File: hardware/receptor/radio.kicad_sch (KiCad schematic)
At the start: 5 parts, among them U2 E220-900T30D

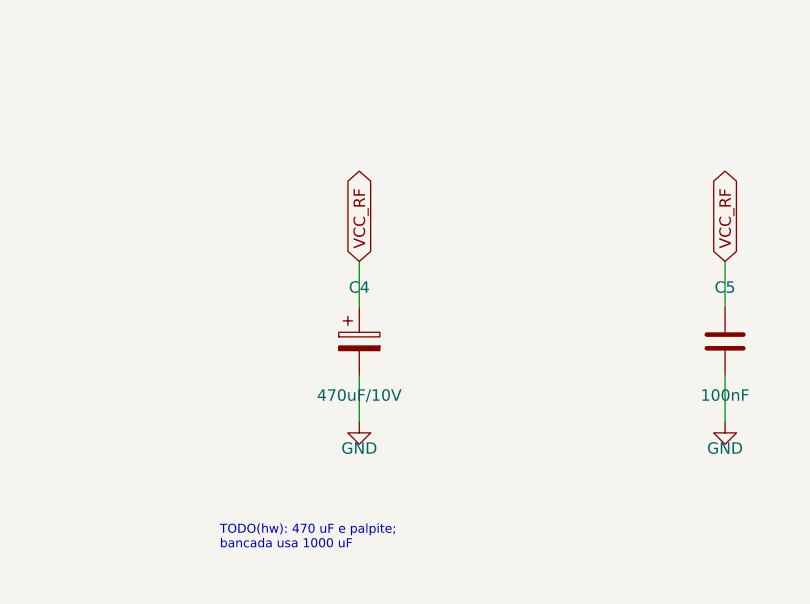
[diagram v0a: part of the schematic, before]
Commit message: wip(hw): roteador proprio, layout v2 com pecas sob o E220 (checkpoint antes de trocar para jack 12 V)
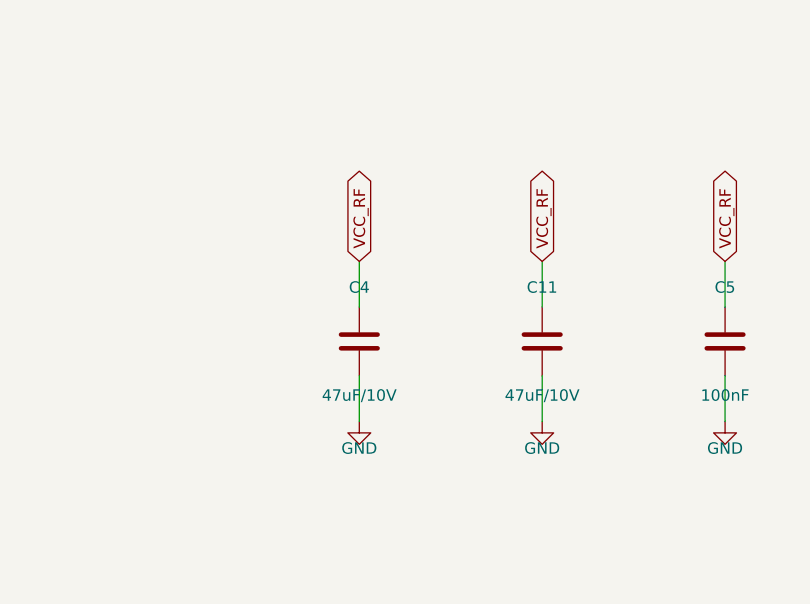
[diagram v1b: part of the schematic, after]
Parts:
- removed C4: 470uF/10V, Capacitor_SMD:CP_Elec_8x10.5, symbol Device:C_Polarized
- added C11, C4: 47uF/10V, Capacitor_SMD:C_1210_3225Metric, symbol Device:C
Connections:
- net GND: now also C11.2, C4.2
- net VCC_RF: now also C11.1, C4.1
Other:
- note removed: "TODO(hw): 470 uF e palpite; bancada usa 1000 uF"

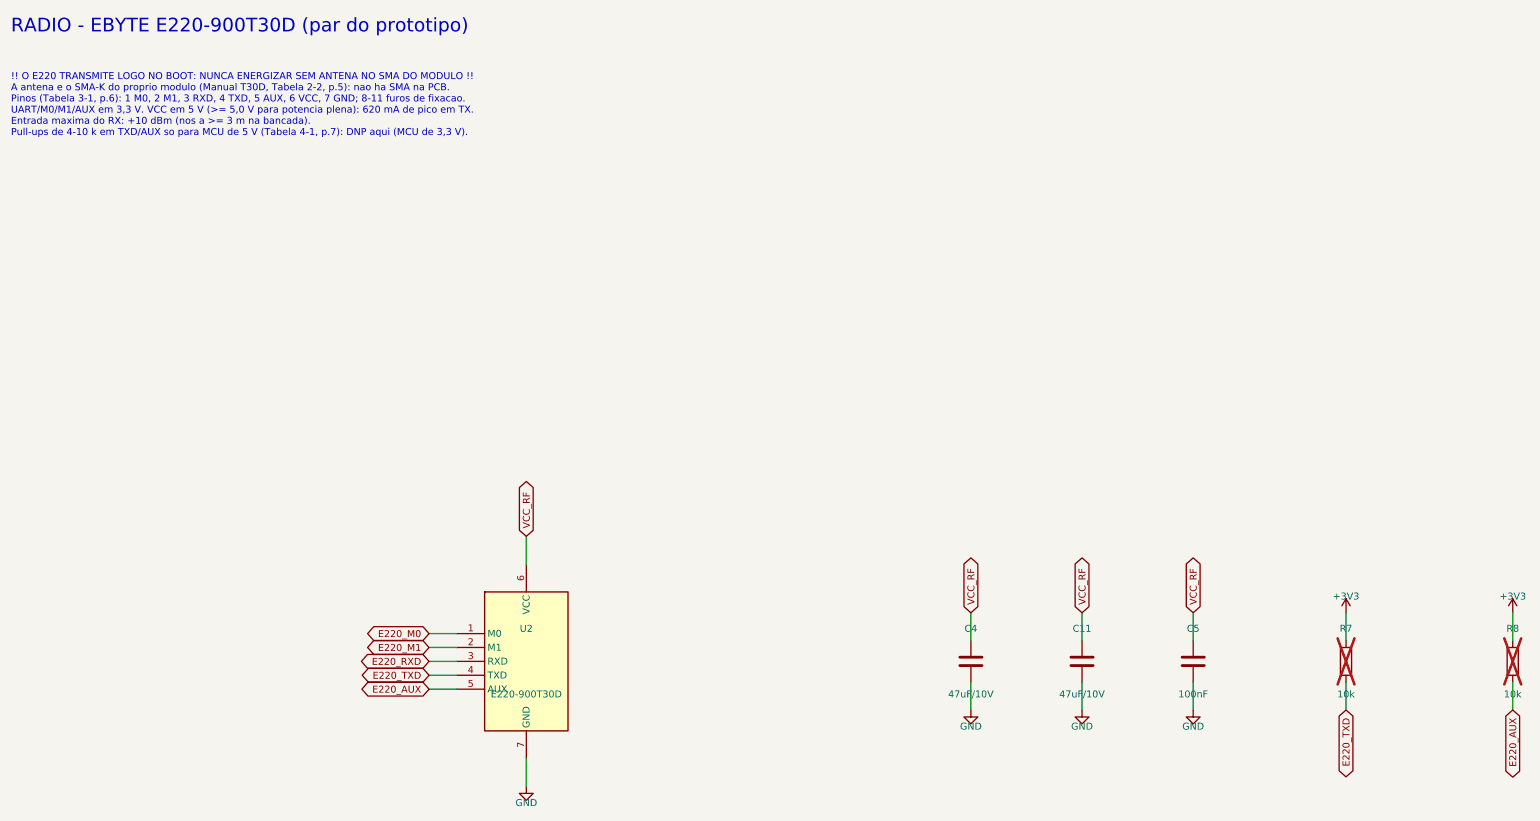
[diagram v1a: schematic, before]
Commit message: feat(hw): jack 12 V com buck AP63205, roteador proprio e serigrafia padronizada (receptor roteado; emissor com 1 net aberta)
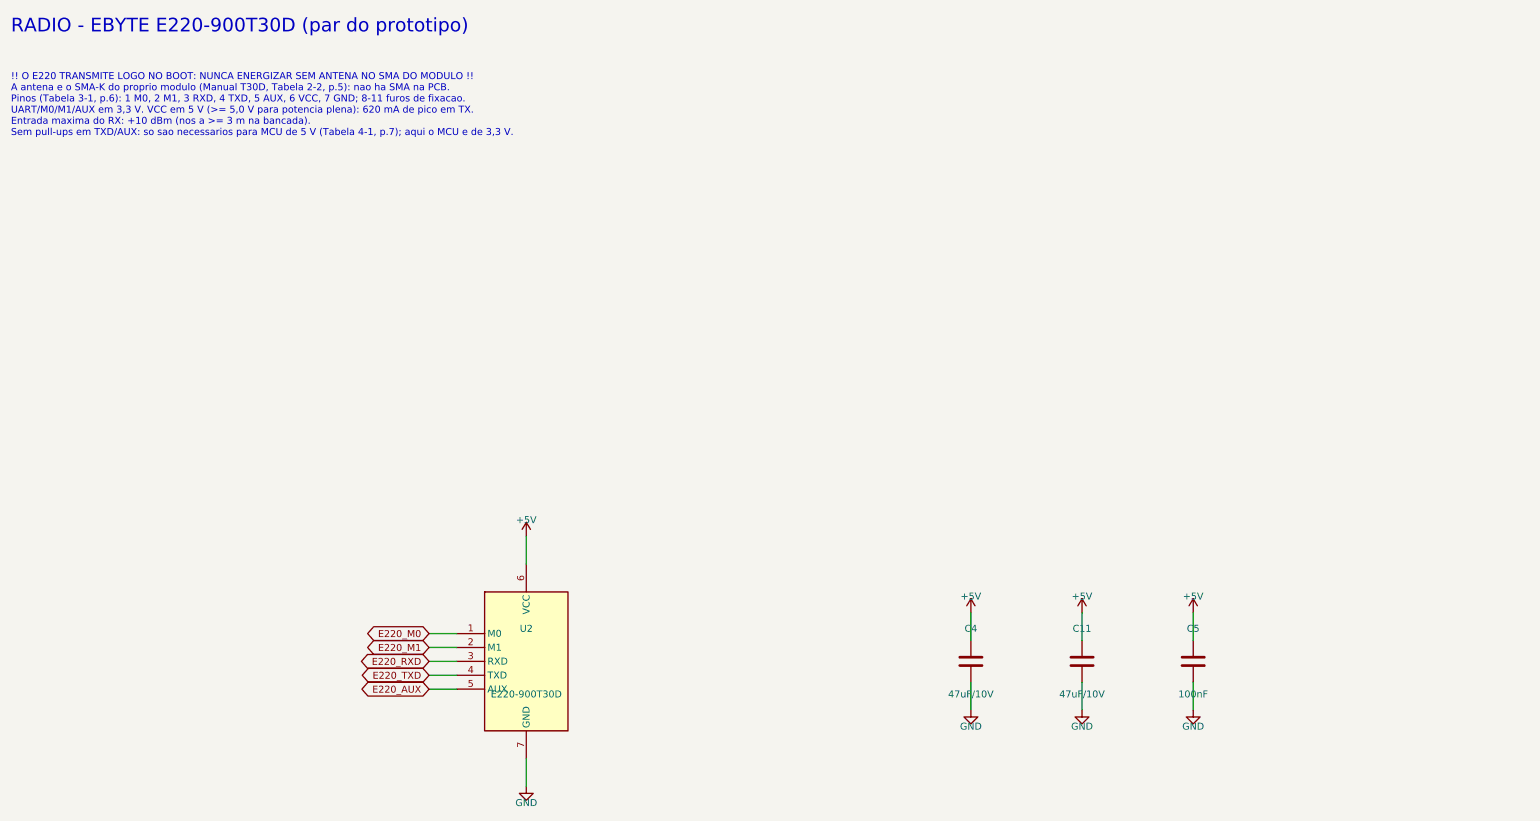
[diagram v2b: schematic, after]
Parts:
- removed R7, R8: 10k, Resistor_SMD:R_0603_1608Metric, symbol Device:R
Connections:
- net VCC_RF renamed +5V
